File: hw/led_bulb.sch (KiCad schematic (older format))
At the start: 112 parts, among them P1 USB_OTG, P10 CONN_01X02, P11 CONN_01X02, P12 CONN_01X02, P13 CONN_01X02, P14 CONN_01X02, P15 CONN_01X02, P16 CONN_01X02, P17 CONN_01X02, P18 CONN_01X02, P19 CONN_01X02, P2 CONN_01X02, P20 CONN_01X02, P21 CONN_01X02, P22 CONN_01X02, P23 CONN_01X02, P24 CONN_01X02, P25 CONN_01X02, P26 CONN_01X02, P27 CONN_01X02, P28 CONN_01X02, P29 CONN_01X02, P3 CONN_01X02, P30 CONN_01X02, P31 CONN_01X02, P32 CONN_01X02, P33 CONN_01X02, P4 CONN_01X02, P5 CONN_01X02, P6 CONN_01X02, P7 CONN_01X02, P8 CONN_01X02, P9 CONN_01X02, Q1 Q_NPN_EBC, Q2 Q_NPN_EBC, SW1 RST, SW2 FLASH, U1 CP2102, U3 ESP-12E, U4 AP1117D33

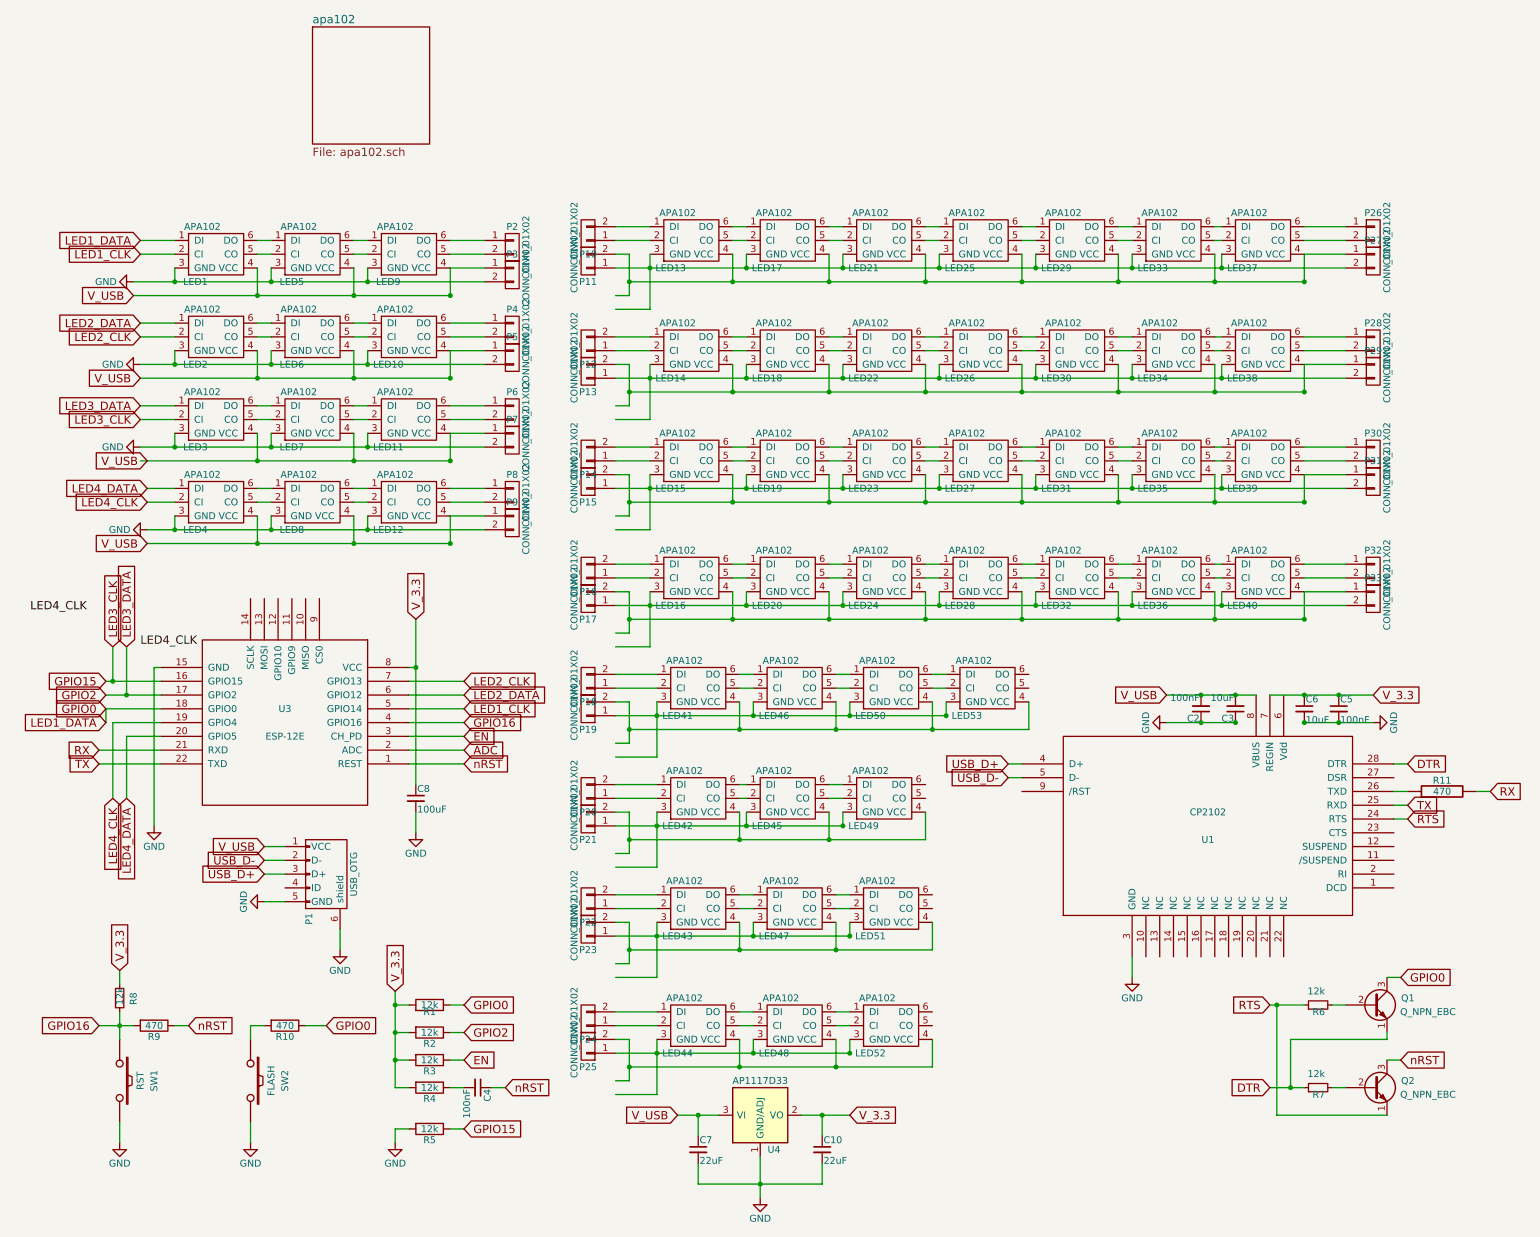
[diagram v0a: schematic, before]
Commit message: Started work on v4.1 of hardware
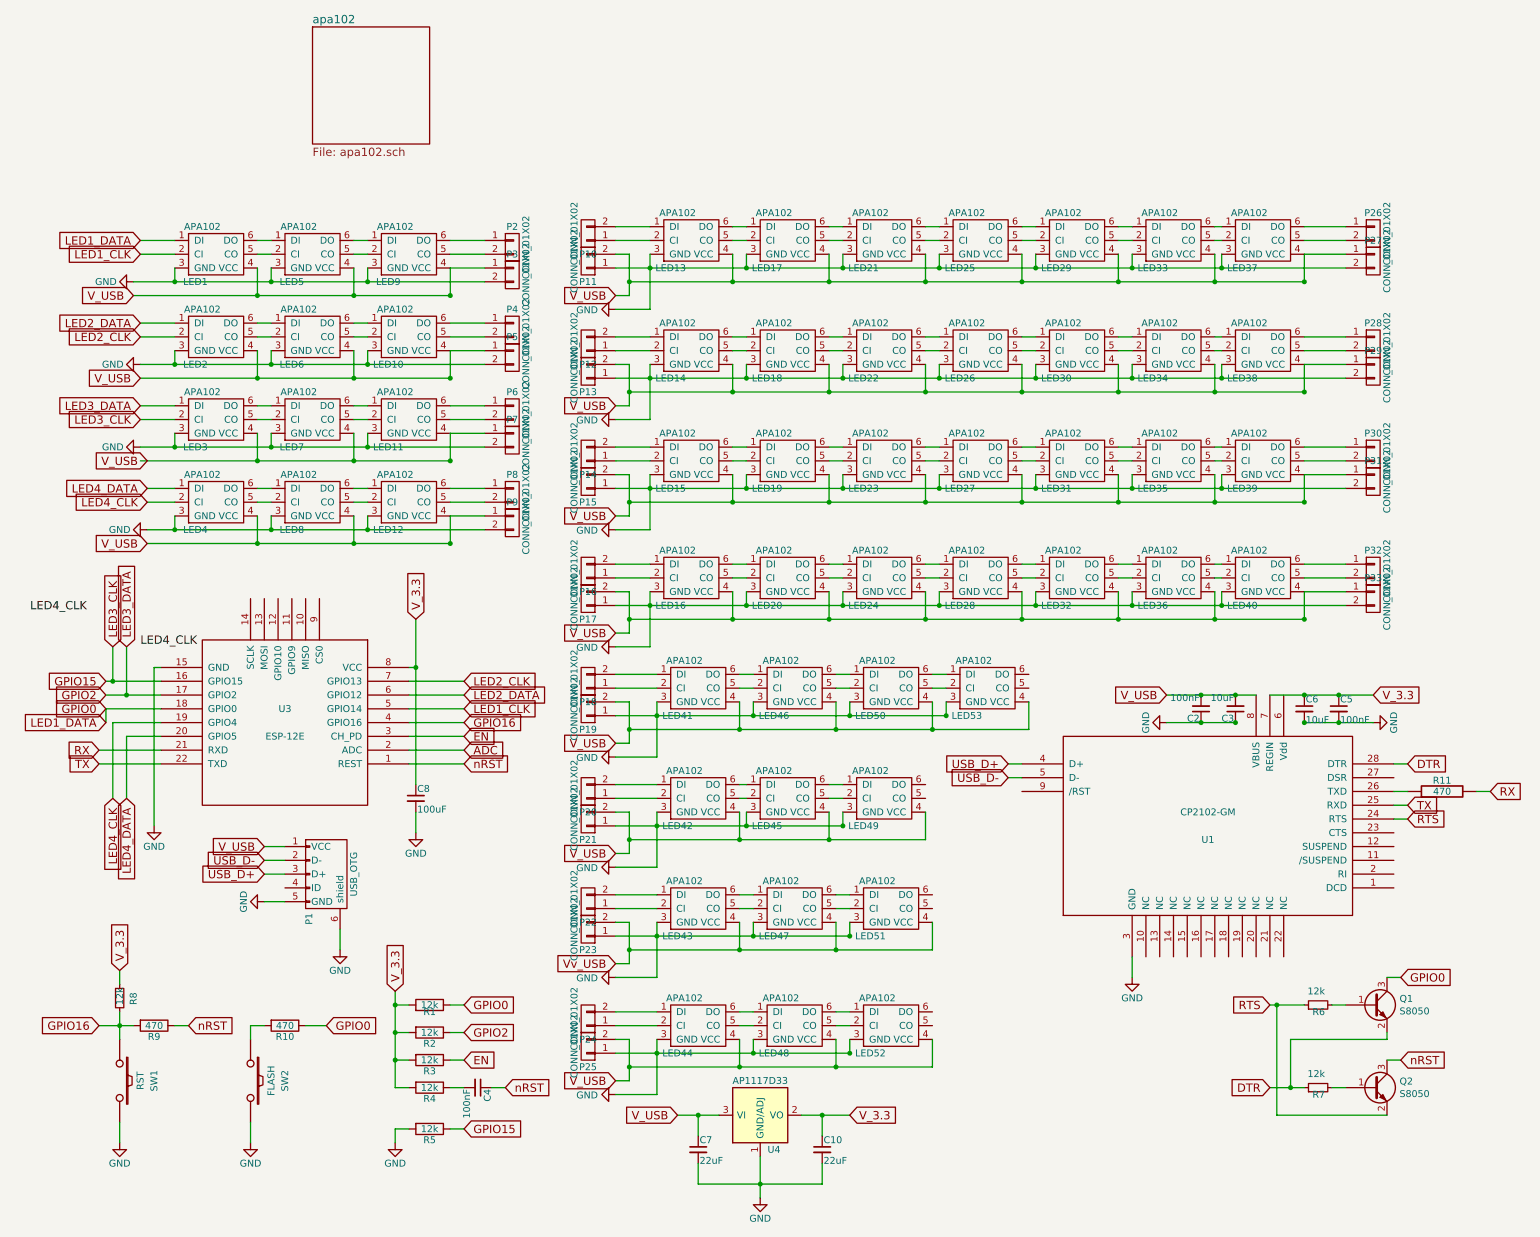
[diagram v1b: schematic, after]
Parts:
- removed Q1, Q2: Q_NPN_EBC, TO_SOT_Packages_SMD:SOT-23, symbol Q_NPN_EBC
- added Q1, Q2: S8050, symbol Q_NPN_BEC
- C10, C7, C8: footprint Capacitors_SMD:C_0603 -> Capacitors_SMD:C_0805
- U1: value CP2102 -> CP2102-GM
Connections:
- net labels added: Vv_USB
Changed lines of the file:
@@
 F 0 "C8" H 3260 4820 50  0000 L CNN
 F 1 "100uF" H 3260 4670 50  0000 L CNN
-F 2 "Capacitors_SMD:C_0603" H 3250 4750 60  0001 C CNN
+F 2 "Capacitors_SMD:C_0805" H 3250 4750 60  0001 C CNN
 F 3 "" H 3250 4750 60  0000 C CNN
 	1    3250 4750
@@
 P 9000 4950
 F 0 "U1" H 9000 4850 50  0000 C CNN
-F 1 "CP2102" H 9000 5050 50  0000 C CNN
+F 1 "CP2102-GM" H 9000 5050 50  0000 C CNN
 F 2 "Housings_DFN_QFN:QFN-28-1EP_5x5mm_Pitch0.5mm" H 9000 4950 60  0001 C CNN
 F 3 "" H 9000 4950 60  0000 C CNN
@@
 F 0 "C7" H 5310 7370 50  0000 L CNN
 F 1 "22uF" H 5310 7220 50  0000 L CNN
-F 2 "Capacitors_SMD:C_0603" H 5300 7300 60  0001 C CNN
+F 2 "Capacitors_SMD:C_0805" H 5300 7300 60  0001 C CNN
 F 3 "" H 5300 7300 60  0000 C CNN
 	1    5300 7300
@@
 F 0 "C10" H 6210 7370 50  0000 L CNN
 F 1 "22uF" H 6210 7220 50  0000 L CNN
-F 2 "Capacitors_SMD:C_0603" H 6200 7300 60  0001 C CNN
+F 2 "Capacitors_SMD:C_0805" H 6200 7300 60  0001 C CNN
 F 3 "" H 6200 7300 60  0000 C CNN
 	1    6200 7300
@@
 $EndComp
 $Comp
-L Q_NPN_EBC Q1
-U 1 1 56E3F2BE
-P 10200 6250
-F 0 "Q1" H 10500 6300 50  0000 R CNN
-F 1 "Q_NPN_EBC" H 10800 6200 50  0000 R CNN
-F 2 "TO_SOT_Packages_SMD:SOT-23" H 10400 6350 50  0001 C CNN
-F 3 "" H 10200 6250 50  0000 C CNN
-	1    10200 6250
-	1    0    0    -1
-$EndComp
-$Comp
-L Q_NPN_EBC Q2
-U 1 1 56E3F86E
-P 10200 6850
-F 0 "Q2" H 10500 6900 50  0000 R CNN
-F 1 "Q_NPN_EBC" H 10800 6800 50  0000 R CNN
-F 2 "TO_SOT_Packages_SMD:SOT-23" H 10400 6950 50  0001 C CNN
-F 3 "" H 10200 6850 50  0000 C CNN
-	1    10200 6850
-	1    0    0    -1
-$EndComp
-$Comp
 L R_Small R7
 U 1 1 56E413BE
@@
 F1 "apa102.sch" 60
 $EndSheet
+$Comp
+L Q_NPN_BEC Q2
+U 1 1 57AF6AAE
+P 10200 6850
+F 0 "Q2" H 10391 6896 50  0000 L CNN
+F 1 "S8050" H 10391 6805 50  0000 L CNN
+F 2 "" H 10400 6950 50  0000 C CNN
+F 3 "" H 10200 6850 50  0000 C CNN
+	1    10200 6850
+	1    0    0    -1
+$EndComp
+$Comp
+L Q_NPN_BEC Q1
+U 1 1 57AF6E24
+P 10200 6250
+F 0 "Q1" H 10391 6296 50  0000 L CNN
+F 1 "S8050" H 10391 6205 50  0000 L CNN
+F 2 "" H 10400 6350 50  0000 C CNN
+F 3 "" H 10200 6250 50  0000 C CNN
+	1    10200 6250
+	1    0    0    -1
+$EndComp
+$Comp
+L GND #PWR?
+U 1 1 57AFA1FA
+P 4700 1200
+F 0 "#PWR?" H 4700 950 50  0001 C CNN
+F 1 "GND" V 4705 1072 50  0000 R CNN
+F 2 "" H 4700 1200 50  0000 C CNN
+F 3 "" H 4700 1200 50  0000 C CNN
+	1    4700 1200
+	0    1    1    0
+$EndComp
+$Comp
+L GND #PWR?
+U 1 1 57AFA35E
+P 4700 2000
+F 0 "#PWR?" H 4700 1750 50  0001 C CNN
+F 1 "GND" V 4705 1872 50  0000 R CNN
+F 2 "" H 4700 2000 50  0000 C CNN
+F 3 "" H 4700 2000 50  0000 C CNN
+	1    4700 2000
+	0    1    1    0
+$EndComp
+$Comp
+L GND #PWR?
+U 1 1 57AFA5A2
+P 4700 2800
+F 0 "#PWR?" H 4700 2550 50  0001 C CNN
+F 1 "GND" V 4705 2672 50  0000 R CNN
+F 2 "" H 4700 2800 50  0000 C CNN
+F 3 "" H 4700 2800 50  0000 C CNN
+	1    4700 2800
+	0    1    1    0
+$EndComp
+$Comp
+L GND #PWR?
+U 1 1 57AFA706
+P 4700 3650
+F 0 "#PWR?" H 4700 3400 50  0001 C CNN
+F 1 "GND" V 4705 3522 50  0000 R CNN
+F 2 "" H 4700 3650 50  0000 C CNN
+F 3 "" H 4700 3650 50  0000 C CNN
+	1    4700 3650
+	0    1    1    0
+$EndComp
+$Comp
+L GND #PWR?
+U 1 1 57AFA86A
+P 4700 4450
+F 0 "#PWR?" H 4700 4200 50  0001 C CNN
+F 1 "GND" V 4705 4322 50  0000 R CNN
+F 2 "" H 4700 4450 50  0000 C CNN
+F 3 "" H 4700 4450 50  0000 C CNN
+	1    4700 4450
+	0    1    1    0
+$EndComp
+$Comp
+L GND #PWR?
+U 1 1 57AFAB8E
+P 4700 5250
+F 0 "#PWR?" H 4700 5000 50  0001 C CNN
+F 1 "GND" V 4705 5122 50  0000 R CNN
+F 2 "" H 4700 5250 50  0000 C CNN
+F 3 "" H 4700 5250 50  0000 C CNN
+	1    4700 5250
+	0    1    1    0
+$EndComp
+$Comp
+L GND #PWR?
+U 1 1 57AFACF2
+P 4700 6050
+F 0 "#PWR?" H 4700 5800 50  0001 C CNN
+F 1 "GND" V 4705 5922 50  0000 R CNN
+F 2 "" H 4700 6050 50  0000 C CNN
+F 3 "" H 4700 6050 50  0000 C CNN
+	1    4700 6050
+	0    1    1    0
+$EndComp
+$Comp
+L GND #PWR?
+U 1 1 57AFAE56
+P 4700 6900
+F 0 "#PWR?" H 4700 6650 50  0001 C CNN
+F 1 "GND" V 4705 6772 50  0000 R CNN
+F 2 "" H 4700 6900 50  0000 C CNN
+F 3 "" H 4700 6900 50  0000 C CNN
+	1    4700 6900
+	0    1    1    0
+$EndComp
+Text GLabel 4700 6800 0    60   Input ~ 0
+V_USB
+Text GLabel 4700 5950 0    60   Input ~ 0
+Vv_USB
+Text GLabel 4700 5150 0    60   Input ~ 0
+V_USB
+Text GLabel 4700 4350 0    60   Input ~ 0
+V_USB
+Text GLabel 4700 3550 0    60   Input ~ 0
+V_USB
+Text GLabel 4700 2700 0    60   Input ~ 0
+V_USB
+Text GLabel 4700 1900 0    60   Input ~ 0
+V_USB
+Text GLabel 4700 1100 0    60   Input ~ 0
+V_USB
 $EndSCHEMATC
